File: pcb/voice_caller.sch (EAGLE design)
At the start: 32 parts, among them IC1 PRO_MICRO, IC2 AT45DB321D-S, IC3 78L12SMD, K1 TQ2SA-L2-5V

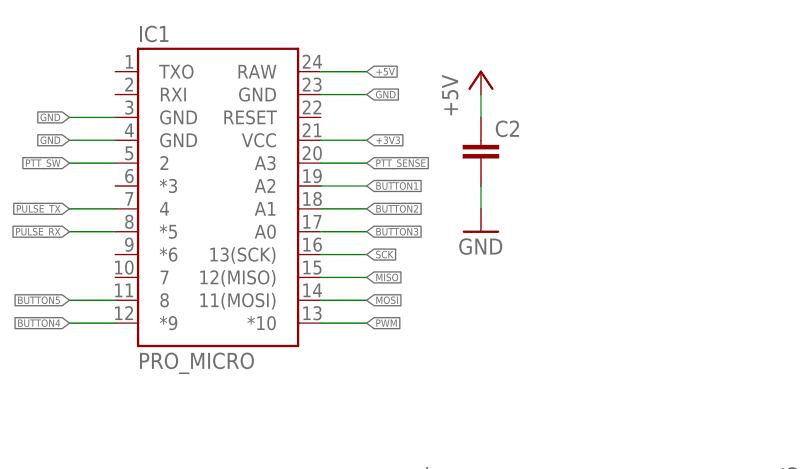
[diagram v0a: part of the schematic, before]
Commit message: Analog pins modified
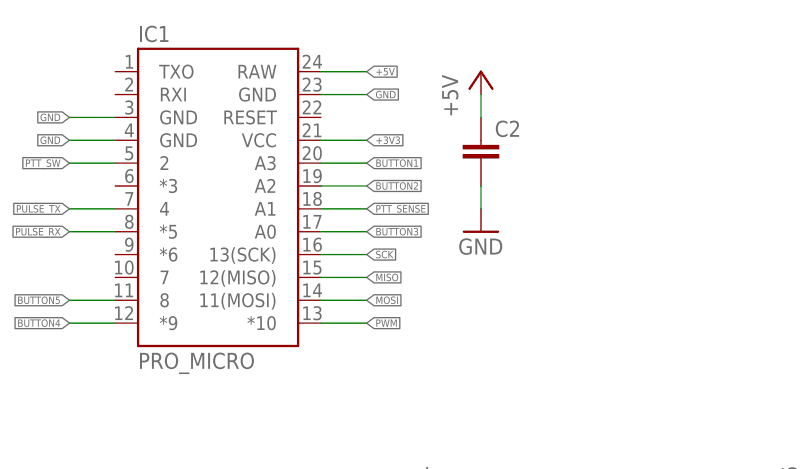
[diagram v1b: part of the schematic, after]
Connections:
- net BUTTON1: now also IC1.A3; no longer IC1.A2
- net BUTTON2: now also IC1.A2; no longer IC1.A1
- net PTT_SENSE: now also IC1.A1; no longer IC1.A3
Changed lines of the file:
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@@
 </segment>
 <segment>
-<pinref part="IC1" gate="G$1" pin="A1"/>
-<wire x1="60.96" y1="142.24" x2="66.04" y2="142.24" width="0.1524" layer="91"/>
-<label x="66.04" y="142.24" size="0.8128" layer="95" xref="yes"/>
+<pinref part="IC1" gate="G$1" pin="A2"/>
+<wire x1="60.96" y1="144.78" x2="66.04" y2="144.78" width="0.1524" layer="91"/>
+<label x="66.04" y="144.78" size="0.8128" layer="95" xref="yes"/>
 </segment>
 </net>
@@
 </segment>
 <segment>
-<pinref part="IC1" gate="G$1" pin="A2"/>
-<wire x1="60.96" y1="144.78" x2="66.04" y2="144.78" width="0.1524" layer="91"/>
-<label x="66.04" y="144.78" size="0.8128" layer="95" xref="yes"/>
-</segment>
-</net>
-<net name="PTT_SENSE" class="0">
-<segment>
 <pinref part="IC1" gate="G$1" pin="A3"/>
 <wire x1="60.96" y1="147.32" x2="66.04" y2="147.32" width="0.1524" layer="91"/>
 <label x="66.04" y="147.32" size="0.8128" layer="95" xref="yes"/>
 </segment>
+</net>
+<net name="PTT_SENSE" class="0">
 <segment>
 <pinref part="T1" gate="G$1" pin="E"/>
@@
 <label x="86.36" y="63.5" size="0.8128" layer="95" xref="yes"/>
 </segment>
+<segment>
+<pinref part="IC1" gate="G$1" pin="A1"/>
+<wire x1="60.96" y1="142.24" x2="66.04" y2="142.24" width="0.1524" layer="91"/>
+<label x="66.04" y="142.24" size="0.8128" layer="95" xref="yes"/>
+</segment>
 </net>

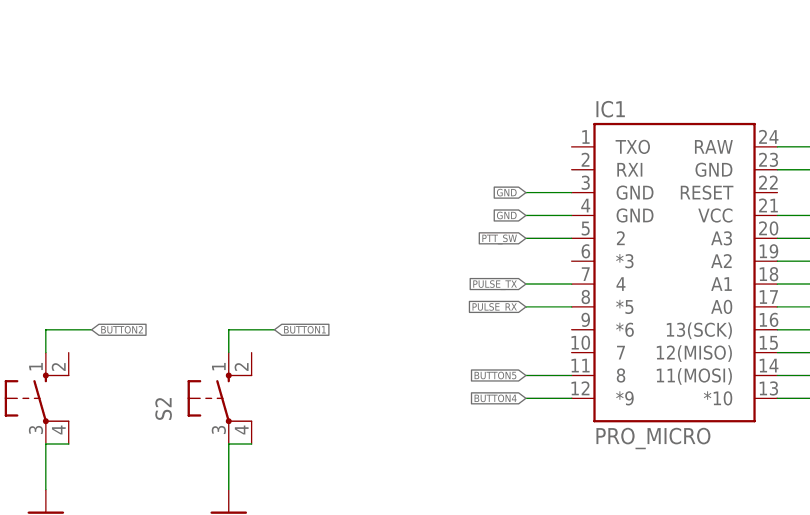
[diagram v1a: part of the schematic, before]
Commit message: Headers for LEDs added
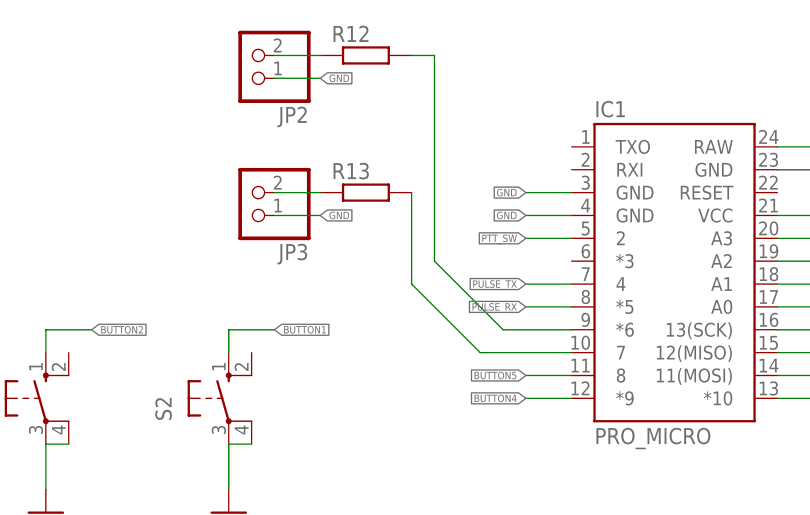
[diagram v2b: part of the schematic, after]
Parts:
- added JP2, JP3: (no value), pinhead:PINHD-1X2
- added R12, R13: (no value), rcl:R-EU_M1206
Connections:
- new net N$12: IC1.*6, R12.2
- new net N$15: IC1.7, R13.2
- new net N$4: JP2.2, R12.1
- new net N$9: JP3.2, R13.1
- net GND: now also JP2.1, JP3.1
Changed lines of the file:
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@@
 <part name="R7" library="rcl" deviceset="R-EU_" device="M1206"/>
 <part name="GND19" library="supply1" deviceset="GND" device=""/>
+<part name="R12" library="rcl" deviceset="R-EU_" device="M1206"/>
+<part name="R13" library="rcl" deviceset="R-EU_" device="M1206"/>
+<part name="JP2" library="pinhead" deviceset="PINHD-1X2" device=""/>
+<part name="JP3" library="pinhead" deviceset="PINHD-1X2" device=""/>
 </parts>
 <sheets>
@@
 <instance part="R7" gate="G$1" x="76.2" y="55.88" rot="R270"/>
 <instance part="GND19" gate="1" x="76.2" y="45.72"/>
+<instance part="R12" gate="G$1" x="15.24" y="167.64"/>
+<instance part="R13" gate="G$1" x="15.24" y="152.4"/>
+<instance part="JP2" gate="G$1" x="2.54" y="167.64" rot="R180"/>
+<instance part="JP3" gate="G$1" x="2.54" y="152.4" rot="R180"/>
 </instances>
 <busses>
@@
 <wire x1="76.2" y1="48.26" x2="76.2" y2="50.8" width="0.1524" layer="91"/>
 </segment>
+<segment>
+<wire x1="5.08" y1="165.1" x2="10.16" y2="165.1" width="0.1524" layer="91"/>
+<label x="10.16" y="165.1" size="0.8128" layer="95" xref="yes"/>
+<pinref part="JP2" gate="G$1" pin="1"/>
+</segment>
+<segment>
+<wire x1="5.08" y1="149.86" x2="10.16" y2="149.86" width="0.1524" layer="91"/>
+<label x="10.16" y="149.86" size="0.8128" layer="95" xref="yes"/>
+<pinref part="JP3" gate="G$1" pin="1"/>
+</segment>
 </net>
 <net name="MOSI" class="0">
@@
 </segment>
 </net>
+<net name="N$4" class="0">
+<segment>
+<pinref part="R12" gate="G$1" pin="1"/>
+<wire x1="5.08" y1="167.64" x2="10.16" y2="167.64" width="0.1524" layer="91"/>
+<pinref part="JP2" gate="G$1" pin="2"/>
+</segment>
+</net>
+<net name="N$9" class="0">
+<segment>
+<pinref part="R13" gate="G$1" pin="1"/>
+<wire x1="5.08" y1="152.4" x2="10.16" y2="152.4" width="0.1524" layer="91"/>
+<pinref part="JP3" gate="G$1" pin="2"/>
+</segment>
+</net>
+<net name="N$12" class="0">
+<segment>
+<pinref part="R12" gate="G$1" pin="2"/>
+<wire x1="20.32" y1="167.64" x2="22.86" y2="167.64" width="0.1524" layer="91"/>
+<wire x1="22.86" y1="167.64" x2="22.86" y2="144.78" width="0.1524" layer="91"/>
+<wire x1="22.86" y1="144.78" x2="30.48" y2="137.16" width="0.1524" layer="91"/>
+<pinref part="IC1" gate="G$1" pin="*6"/>
+<wire x1="30.48" y1="137.16" x2="38.1" y2="137.16" width="0.1524" layer="91"/>
+</segment>
+</net>
+<net name="N$15" class="0">
+<segment>
+<pinref part="R13" gate="G$1" pin="2"/>
+<wire x1="20.32" y1="152.4" x2="20.32" y2="142.24" width="0.1524" layer="91"/>
+<wire x1="20.32" y1="142.24" x2="27.94" y2="134.62" width="0.1524" layer="91"/>
+<pinref part="IC1" gate="G$1" pin="7"/>
+<wire x1="27.94" y1="134.62" x2="38.1" y2="134.62" width="0.1524" layer="91"/>
+</segment>
+</net>

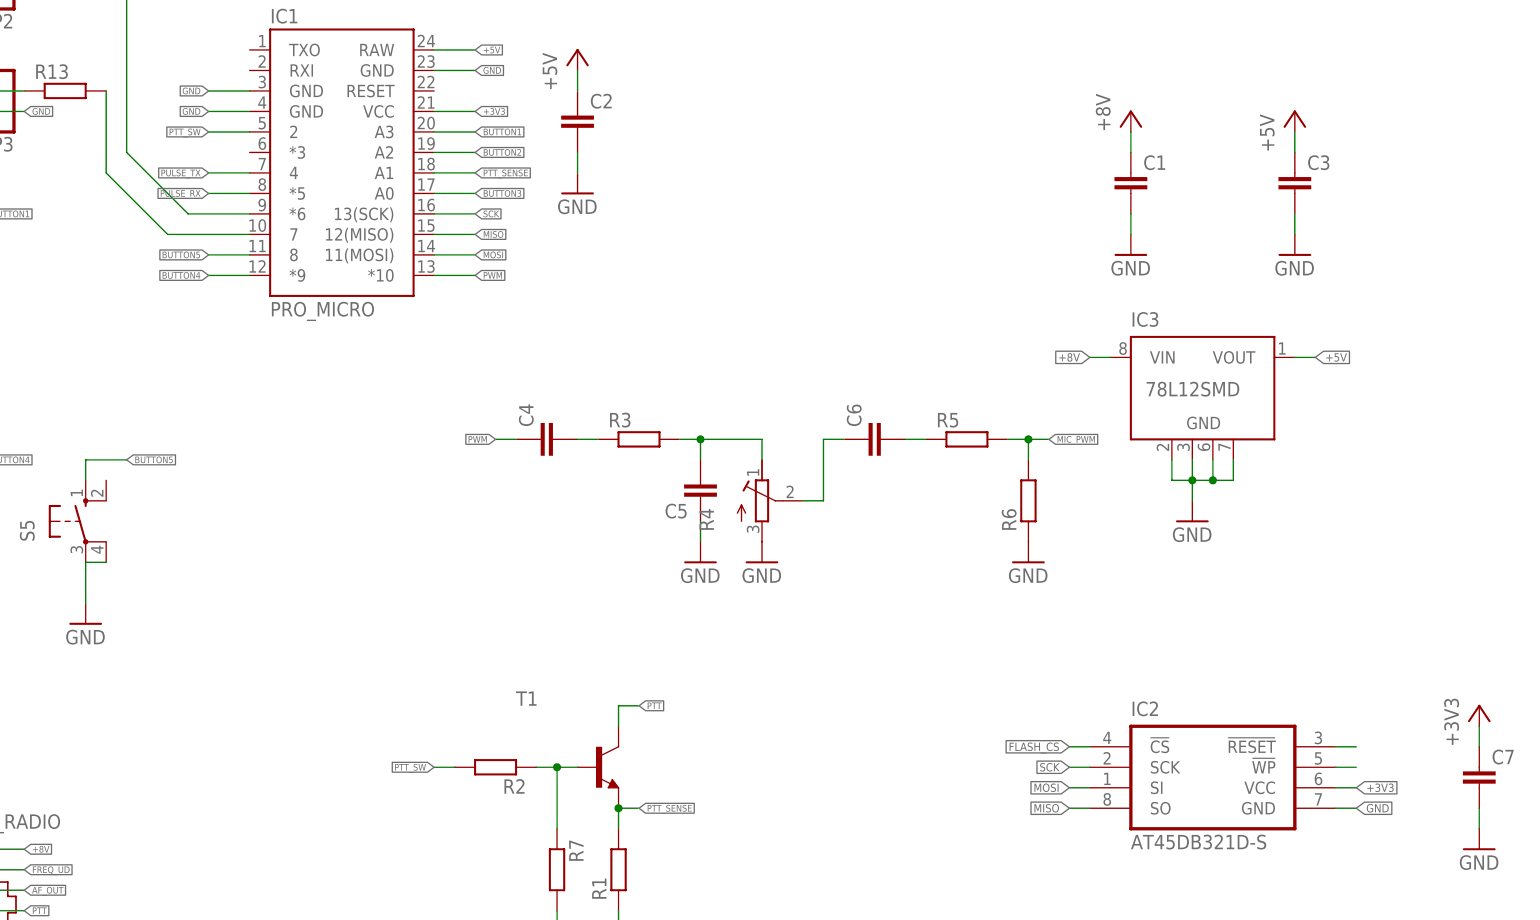
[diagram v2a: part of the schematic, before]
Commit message: Missing nets for flash routed.
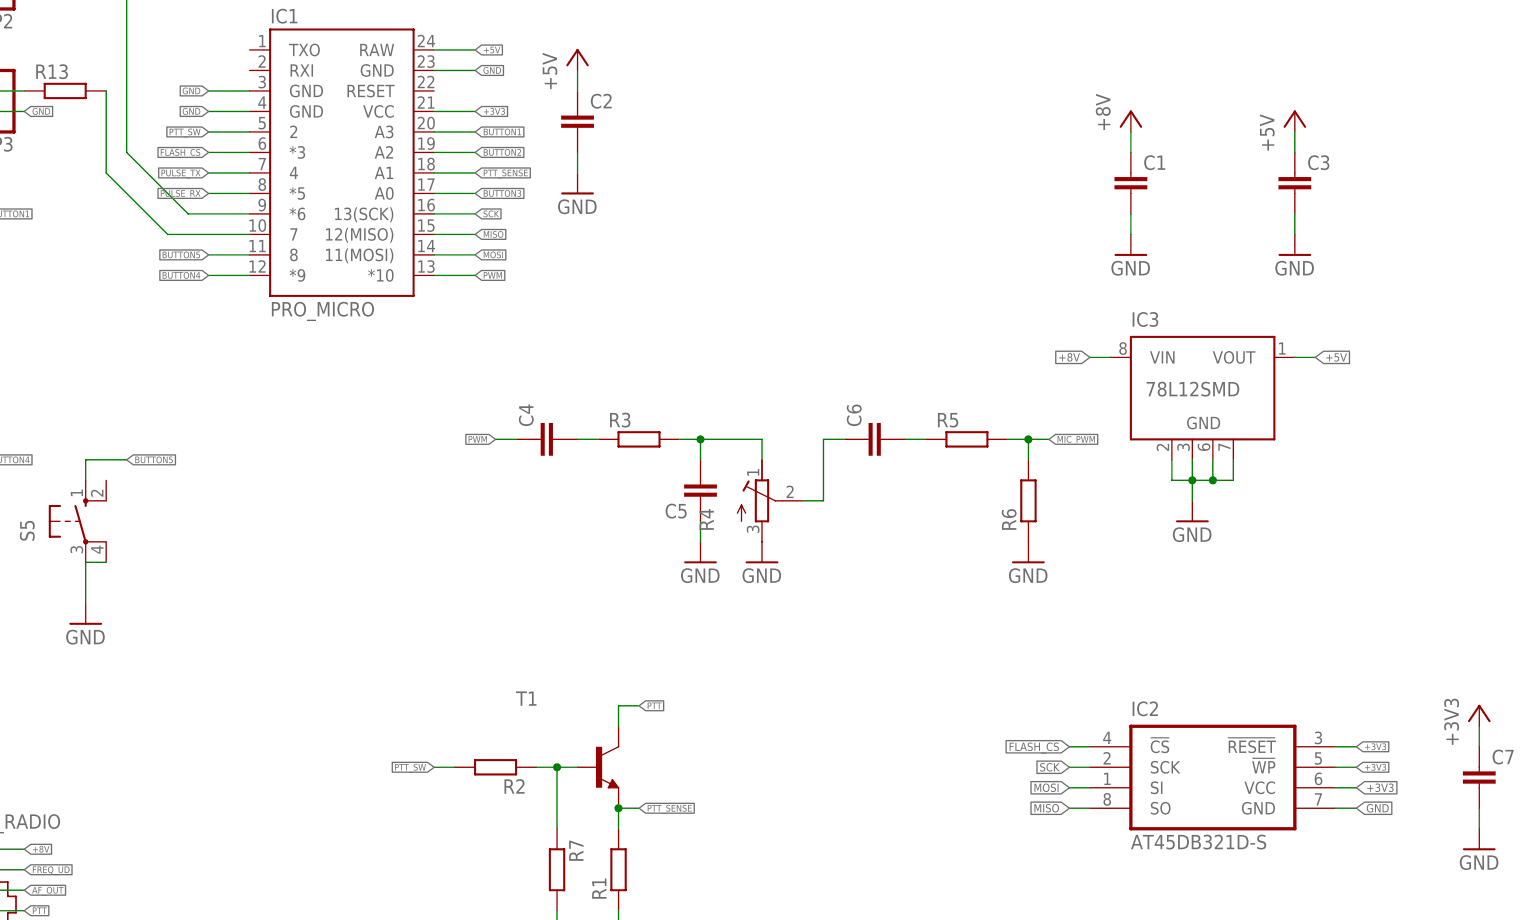
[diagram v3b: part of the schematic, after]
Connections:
- removed net N$7: IC2.!WP!
- removed net N$8: IC2.!RESET!
- net +3V3: now also IC2.!RESET!, IC2.!WP!
- net FLASH_CS: now also IC1.*3
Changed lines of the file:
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@@
 <label x="139.7" y="71.12" size="1.016" layer="95" rot="R180" xref="yes"/>
 </segment>
-</net>
-<net name="N$7" class="0">
 <segment>
-<pinref part="IC2" gate="G$1" pin="!WP!"/>
-<wire x1="172.72" y1="68.58" x2="175.26" y2="68.58" width="0.1524" layer="91"/>
-</segment>
-</net>
-<net name="N$8" class="0">
-<segment>
-<pinref part="IC2" gate="G$1" pin="!RESET!"/>
-<wire x1="172.72" y1="71.12" x2="175.26" y2="71.12" width="0.1524" layer="91"/>
+<pinref part="IC1" gate="G$1" pin="*3"/>
+<wire x1="38.1" y1="144.78" x2="33.02" y2="144.78" width="0.1524" layer="91"/>
+<label x="33.02" y="144.78" size="0.8128" layer="95" rot="R180" xref="yes"/>
 </segment>
 </net>
@@
 <pinref part="+3V1" gate="G$1" pin="+3V3"/>
 </segment>
+<segment>
+<pinref part="IC2" gate="G$1" pin="!RESET!"/>
+<wire x1="172.72" y1="71.12" x2="175.26" y2="71.12" width="0.1524" layer="91"/>
+<label x="175.26" y="71.12" size="0.8128" layer="95" xref="yes"/>
+</segment>
+<segment>
+<pinref part="IC2" gate="G$1" pin="!WP!"/>
+<wire x1="172.72" y1="68.58" x2="175.26" y2="68.58" width="0.1524" layer="91"/>
+<label x="175.26" y="68.58" size="0.8128" layer="95" xref="yes"/>
+</segment>
 </net>
